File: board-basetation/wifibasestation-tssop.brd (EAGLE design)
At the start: 49.8 x 22.5 mm, 22 parts, among them IC1 1117EMP, J1 SWD_SHROUD_SMD, X1 ESP-03, X2 SMA-142-0711-821/826

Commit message: something changed
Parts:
- removed R1: 10k, passives-7351:R0603-N
- removed R6: 4k7, passives-7351:R0603-N
- added JP1: FTDI_BASICPTH, SparkFun-Connectors:FTDI_BASIC
- added RN2: 10k, resistor-dil:EXB38V
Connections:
- removed net N$18: R1.2, S1.1, U$1.1
- new net N$2: RN2.2, S1.1, U$1.1
- new net N$8: RN2.4, X1.6
- net +3V3: now also RN2.5; no longer R6.1
- net GND: now also RN2.6, RN2.7, RN2.8; no longer R1.1
- net GPIO0: now also RN2.1
- net GPIO15: now also RN2.3
- net N$1: no longer R6.2, X1.6
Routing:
- net N$2: track 0.00 -> 33.8 mm, vias 0 -> 2
- net N$18: track 28.0 -> 0.00 mm, vias 2 -> 0
- net GPIO15: track 7.91 -> 14.1 mm, vias 1 -> 2
- net N$1: track 5.50 -> 0.00 mm, vias 1 -> 0
- net N$8: track 0.00 -> 4.97 mm, vias 0 -> 1
- net GND: track 49.1 -> 53.7 mm
- net GPIO0: track 46.7 -> 49.3 mm, vias 1 -> 2
- net +3V3: track 107.8 -> 108.9 mm, vias 13 -> 12

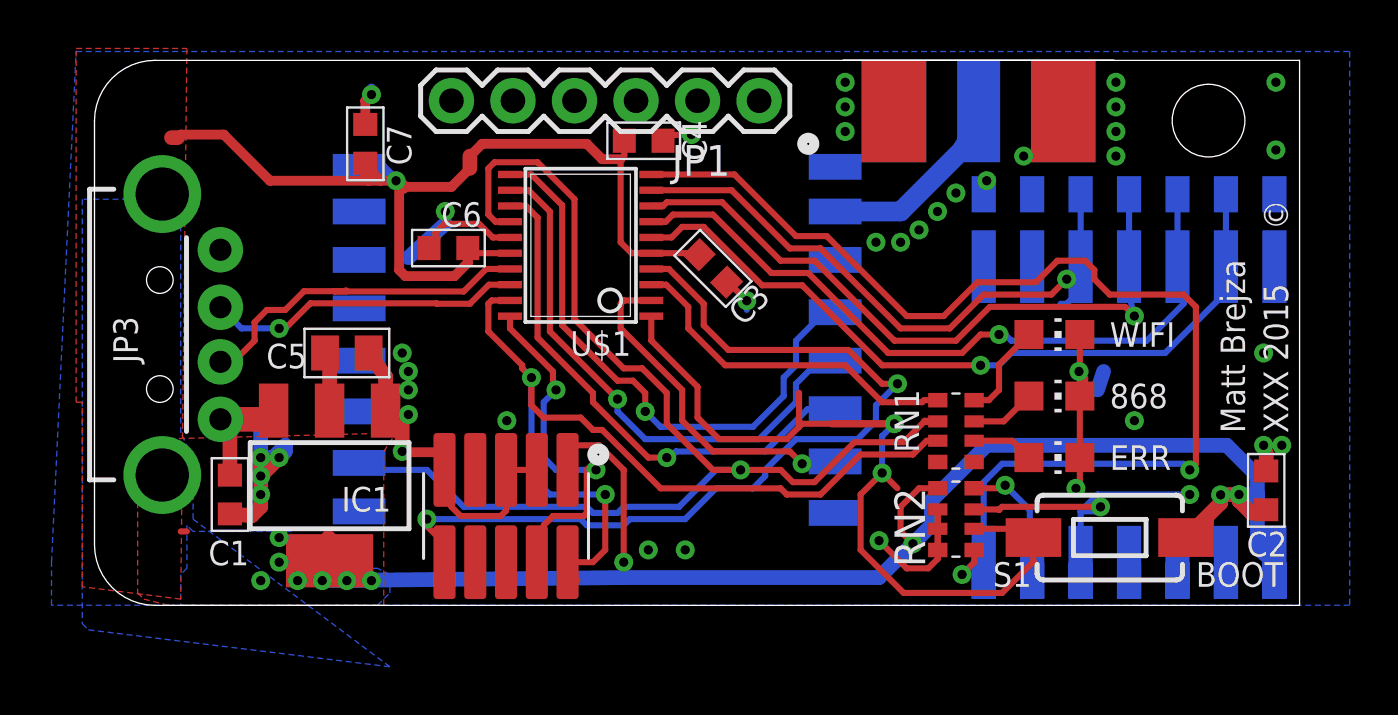
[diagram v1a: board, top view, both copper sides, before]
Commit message: pretty much done tssop version
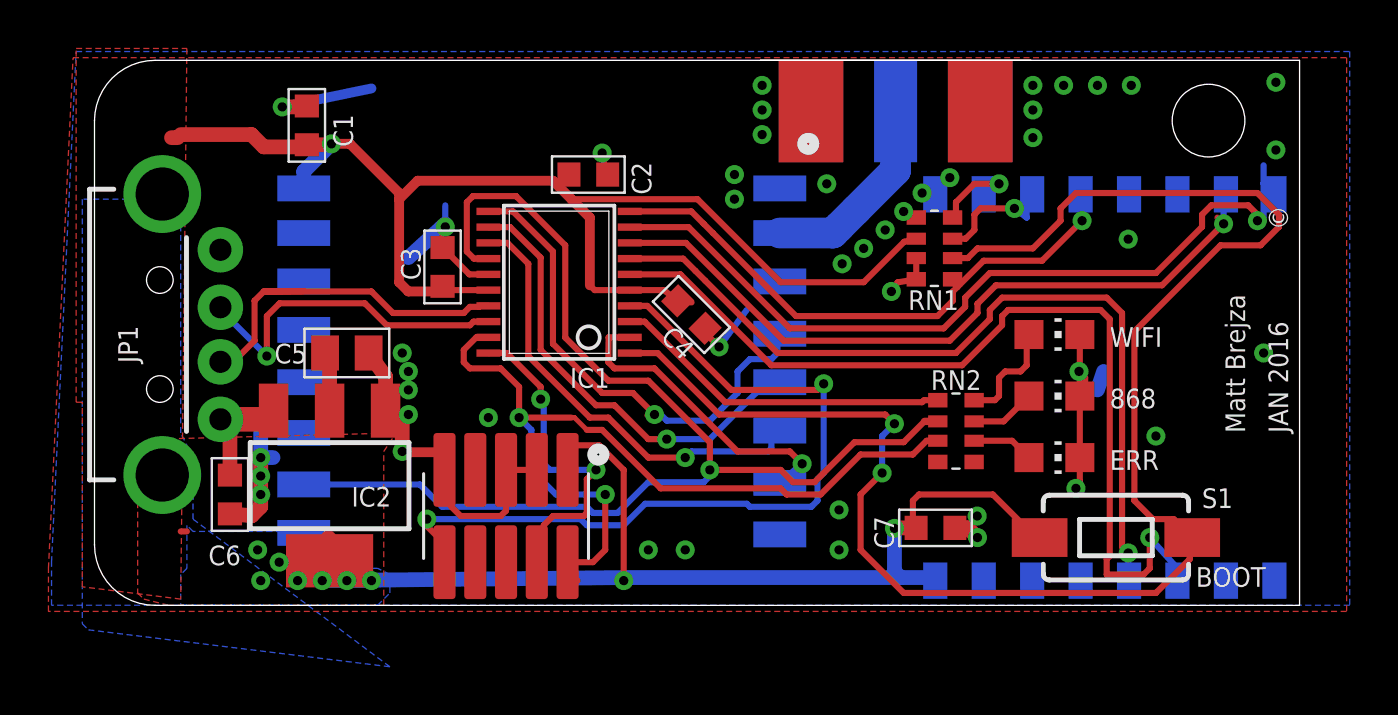
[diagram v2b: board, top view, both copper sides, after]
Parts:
- removed JP3: USB-A-H, SparkFun-Connectors:USB-A-H
- removed U$2: RFM69HW, hoperf:RFM
- removed U$3: ESP-07, Mine:ESP-07
- added IC2: 1117EMP, dtb:SOT223
- C1: value 4u7 -> 1u
- C2, C3: value 1u -> 100n
- C4: value 100n -> 1u
- C6: value 100n -> 4u7
- IC1: value 1117EMP -> STM32F030F4; device dtb:SOT223 -> dtb:TSSOP20
- JP1: value FTDI_BASICPTH -> USB-A-H; device SparkFun-Connectors:FTDI_BASIC -> SparkFun-Connectors:USB-A-H
- RN1: value 330 -> 10k
- RN2: value 10k -> 330
- U$1: value STM32F030F4 -> RFM69HW; device dtb:TSSOP20 -> hoperf:RFM
- X1: value ESP-03 -> ESP-07; device Mine:ESP-03 -> TiLDA Mk3 Parts:ESP-07
- moved C2 30.9 mm to (20.6, 18.0), turned to 0 degrees
- moved C7 28.4 mm to (35.0, 3.45), turned to 0 degrees
- moved JP1 26.5 mm to (3.05, 11.4), turned to 0 degrees
- moved C1 15.6 mm to (9.02, 20.1), turned to 90 degrees
- moved C6 13.6 mm to (5.84, 4.83), turned to 270 degrees
- moved IC1 12.7 mm to (19.4, 13.6), turned to 90 degrees
- moved U$1 11.9 mm to (8.89, 18.5), flipped to the bottom, turned to 180 degrees
- moved C3 11.2 mm to (14.6, 14.2), turned to 90 degrees
- moved RN1 7.59 mm to (34.9, 15.0), turned to 90 degrees
- moved C4 7.44 mm to (24.9, 12.3), turned to 315 degrees
- moved LED1 5.08 mm to (39.9, 11.4)
- moved LED3 5.08 mm to (39.9, 6.35)
- moved RN2 3.64 mm to (35.8, 7.45), turned to 270 degrees
- moved X2 3.43 mm to (33.3, 22.8)
- moved X1 0.76 mm to (35.6, 1.27)
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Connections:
- removed net N$1: U$3.6
- removed net N$3: U$3.2, X1.2
- removed net N$4: U$3.4, X1.4
- removed net N$7: U$3.3, X1.3
- net +3V3: now also C1.1, IC1.16, IC1.5, IC2.2, IC2.4, RN1.6, U$1.VCC, X1.8; no longer C6.1, IC1.2, IC1.4, RN2.5, U$1.16, U$1.5, U$2.VCC, U$3.1, X1.1
- net CH_PD: now also IC1.6, X1.3; no longer U$1.6, U$3.13, X1.13
- net DIO0: now also IC1.14, RN2.2, U$1.DIO0; no longer RN1.2, U$1.14, U$2.DIO0
- net DM: now also IC1.17, JP1.D-; no longer JP3.D-, U$1.17
- net DP: now also IC1.18, JP1.D+; no longer JP3.D+, U$1.18
- net GND: now also IC1.15, IC2.1, JP1.GND, RN1.5, RN1.7, RN1.8, U$1.GNDA, U$1.GNDB, X1.9; no longer IC1.1, JP3.GND, RN2.6, RN2.7, RN2.8, U$1.15, U$2.GNDA, U$2.GNDB, U$3.8, X1.8
- net GPIO0: now also IC1.10, RN1.1, X1.12; no longer RN2.1, U$1.10, U$3.7, X1.7
- net GPIO15: now also RN1.4, X1.10; no longer RN2.3, U$3.5, X1.5
- net MISO: now also IC1.12, U$1.MISO; no longer U$1.12, U$2.MISO
- net MOSI: now also IC1.13, U$1.MOSI; no longer U$1.13, U$2.MOSI
- net N$10: now also RN2.7; no longer RN1.7
- net N$2: now also IC1.1, RN1.2; no longer RN2.2, U$1.1
- net N$20: now also LED3.A, RN2.6; no longer LED1.A, RN1.6
- net N$22: now also IC1.3, RN2.1; no longer RN1.1, U$1.3
- net N$6: now also U$1.ANT; no longer U$2.ANT
- net N$8: now also RN1.3, X1.11; no longer RN2.4, X1.6
- net N$9: now also LED1.A, RN2.8; no longer LED3.A, RN1.8
- net NRST: now also IC1.4; no longer U$1.4
- net NSS: now also IC1.2, U$1.NSS; no longer U$1.2, U$2.NSS
- net RST: now also U$1.RESET; no longer U$2.RESET
- net SCK: now also IC1.11, U$1.SCK; no longer U$1.11, U$2.SCK
- net SWCLK: now also IC1.20; no longer U$1.20
- net SWDAT: now also IC1.19, RN2.3; no longer RN1.3, U$1.19
- net USART_RX: now also IC1.9, X1.16; no longer U$1.9, U$3.10, X1.10
- net USART_TX: now also IC1.8, X1.15; no longer U$1.8, U$3.11, X1.11
- net VBUS: now also C6.1, IC2.3, JP1.VBUS; no longer C1.1, IC1.3, JP3.VBUS
- net W_RST: now also IC1.7, X1.4; no longer U$1.7, U$3.12, X1.12
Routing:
- net N$2: track 33.8 -> 67.3 mm
- net GPIO0: track 49.3 -> 23.9 mm, vias 2 -> 1
- net GPIO15: track 14.1 -> 3.98 mm, vias 2 -> 1
- net USART_RX: track 25.9 -> 33.9 mm
- net +3V3: track 108.9 -> 101.4 mm, vias 12 -> 10
- net CH_PD: track 31.6 -> 38.7 mm
- net W_RST: track 30.1 -> 34.5 mm
- net NRST: track 37.1 -> 33.2 mm
- net GND: track 53.7 -> 49.9 mm, vias 39 -> 45
- net MISO: track 22.7 -> 18.9 mm
- net SCK: track 24.4 -> 20.7 mm
- net MOSI: track 21.7 -> 18.6 mm
- net USART_TX: track 28.5 -> 30.0 mm
- net SWCLK: track 15.7 -> 14.2 mm
- net SWDAT: track 37.5 -> 36.3 mm
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- added copper zone on layer 1, net GND
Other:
- board text added: "JAN 2016"
- board text removed: "Add tape to insulate vias"
- board text removed: "XXX 2015"
